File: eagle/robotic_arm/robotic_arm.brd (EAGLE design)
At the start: 81.3 x 63.5 mm, 98 parts, among them J2 (ID,OD)=(2.1,5.5)MM, SW1 5A/28V, Y1 16MHz

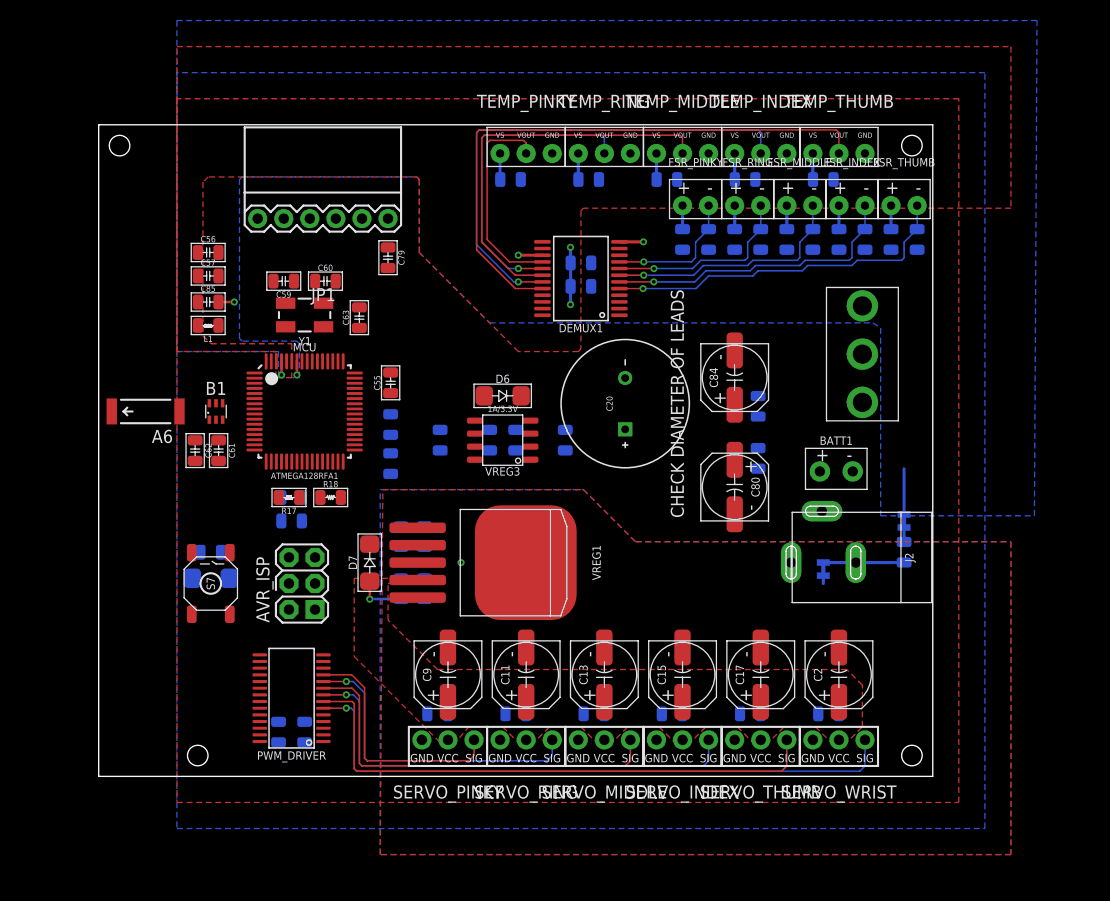
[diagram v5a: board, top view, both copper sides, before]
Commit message: Started on immediate power connections
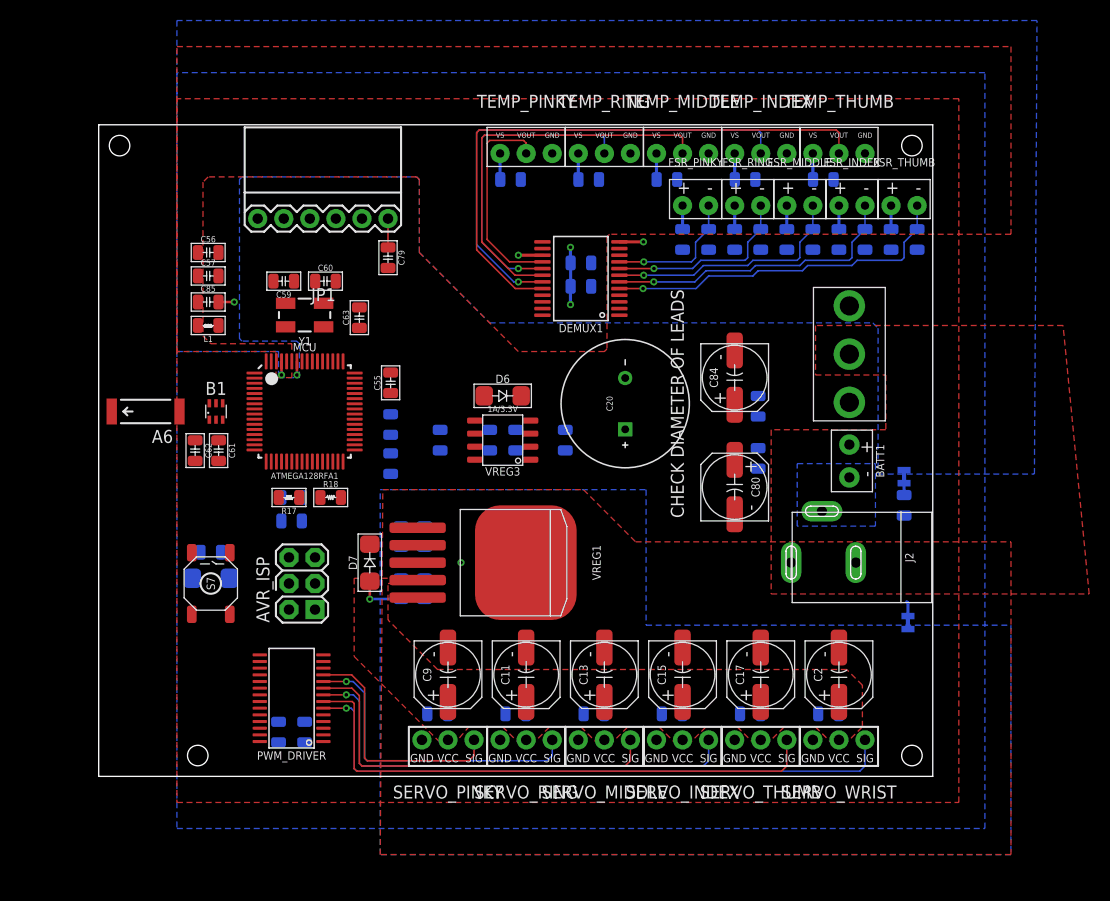
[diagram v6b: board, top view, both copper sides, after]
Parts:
- moved SUPPLY51 9.76 mm to (81.4, 15.0)
- moved L2 4.57 mm to (81.0, 26.4)
- moved SUPPLY52 4.32 mm to (81.0, 29.2)
- moved BATT1 1.63 mm to (75.7, 30.7), turned to 270 degrees
- moved SW1 1.27 mm to (75.7, 41.1)
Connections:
- net N$2 renamed BATT_-
- net N$43 renamed BATT_+
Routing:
- net GND: track 7.87 -> 1.45 mm
- net AGND: track 13.3 -> 9.01 mm
- net N$41: track 0.00 -> 2.81 mm
- net NGND: track 0.77 -> 0.00 mm
- added copper zone on layer 1, net BATT_+
- added copper zone on layer 16, net BATT_-

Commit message: Moved DEMUX to give some more power plane area.
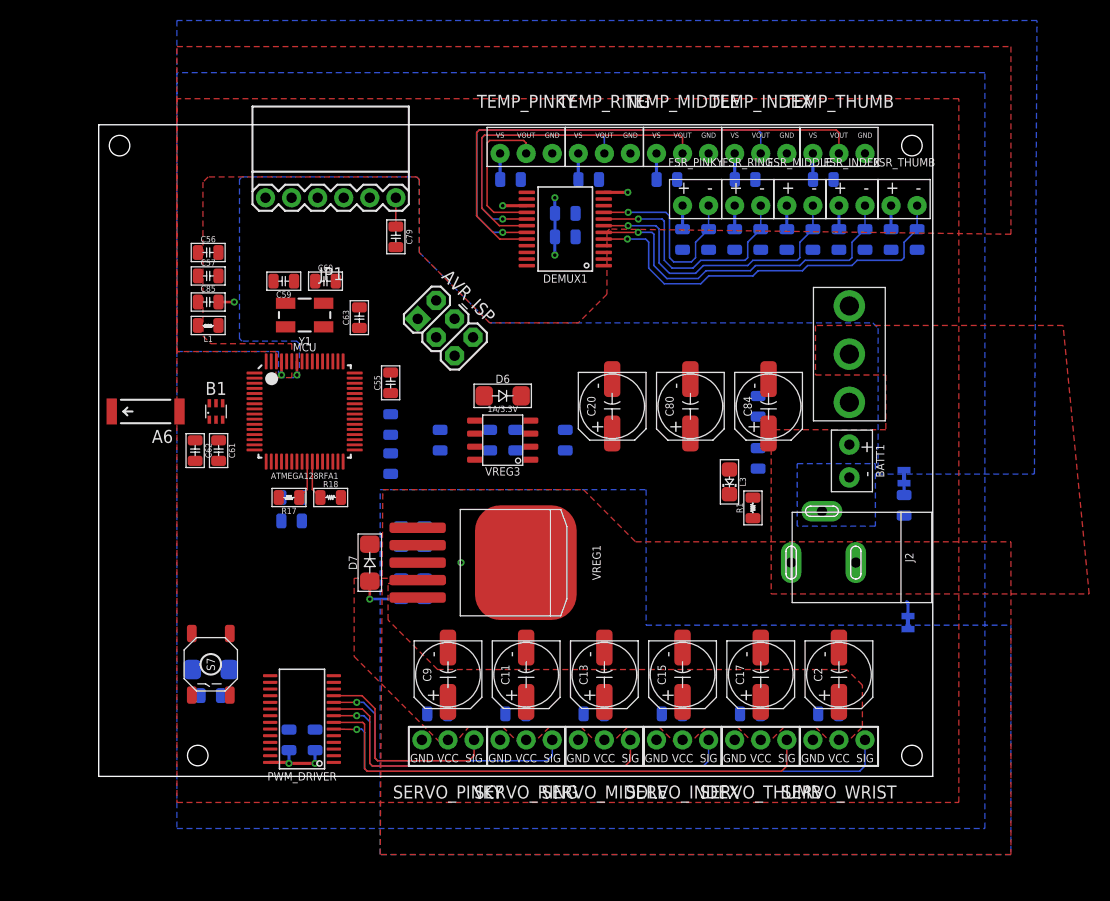
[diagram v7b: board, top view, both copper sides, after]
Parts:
- added L3: BLUE, MrSwirlyEyes:LED_SMD-805_
- added R1: 10KΩ, MrSwirlyEyes:RESISTOR_SMD-805
- C20: value 1000uF/50V -> 220uF/16V; device MrSwirlyEyes:CAP_POL_DIA12.5-LS5-H27 -> MrSwirlyEyes:CAP_POL_SMD_L6.6-W6.6
- moved AVR_ISP 28.5 mm to (36.3, 43.7), turned to 315 degrees
- moved R43 14.0 mm to (13.5, 7.87), turned to 0 degrees
- moved C80 8.98 mm to (60.2, 36.1), turned to 90 degrees
- moved D1 8.89 mm to (13.5, 10.4), turned to 0 degrees
- moved S7 7.87 mm to (13.5, 10.9), turned to 90 degrees
- moved C18 5.06 mm to (48.0, 54.9)
- moved C26 5.06 mm to (48.0, 52.6)
- moved DEMUX1 5.06 mm to (48.0, 53.3)
- moved C84 4.33 mm to (67.8, 36.1)
- moved PWM_DRIVER 2.27 mm to (22.4, 5.59)
- moved C79 2.17 mm to (31.5, 52.6)
- moved JP1 2.17 mm to (31.5, 56.4)
- moved C20 1.30 mm to (52.6, 36.1)
- moved C25 1.27 mm to (21.1, 3.56)
- moved C19 1.27 mm to (23.6, 3.56)
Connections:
- new net N$2: L3.K, R1.2
- net GND: now also C20.K, R1.1; no longer C20.-
- net N$1: now also C20.A, L3.A; no longer C20.+
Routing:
- net VCC: track 0.00 -> 6.98 mm, vias 0 -> 2
- net FSR_PINKY: track 13.2 -> 19.1 mm
- net FSR_RING: track 18.6 -> 24.3 mm
- net TEMP_PINKY: track 56.9 -> 51.5 mm
- net TEMP_THUMB: track 20.7 -> 15.3 mm
- net TEMP_MIDDLE: track 38.7 -> 33.2 mm
- net TEMP_INDEX: track 30.8 -> 25.3 mm
- net FSR_MIDDLE: track 23.9 -> 29.2 mm
- net TEMP_RING: track 48.8 -> 43.6 mm
- net FSR_INDEX: track 29.2 -> 34.3 mm
- net FSR_THUMB: track 34.6 -> 39.2 mm
- net SDA: track 0.00 -> 3.83 mm
- net SCL: track 0.00 -> 3.82 mm
- net SERVO_THUMB: track 31.0 -> 27.9 mm
- net SERVO_RING: track 54.4 -> 51.4 mm
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
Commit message: Routed VBATT and moved MCU regulator for a well-shaped power plane
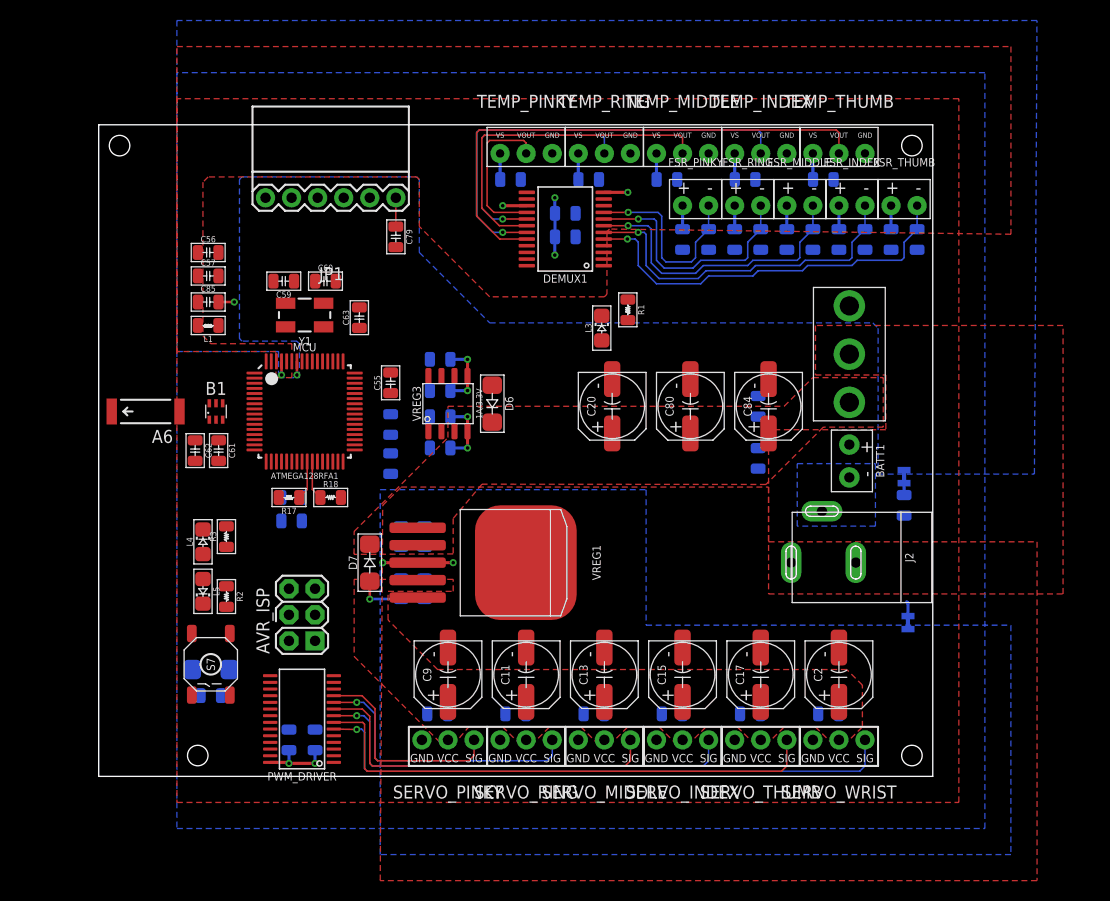
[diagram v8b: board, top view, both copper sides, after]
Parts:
- added L4: GREEN, MrSwirlyEyes:LED_SMD-805_
- added L5: RED, MrSwirlyEyes:LED_SMD-805_
- added R2: 2KΩ, MrSwirlyEyes:RESISTOR_SMD-805
- added R3: 1KΩ, MrSwirlyEyes:RESISTOR_SMD-805
- moved AVR_ISP 31.2 mm to (22.4, 15.7), turned to 90 degrees
- moved R1 22.8 mm to (54.1, 45.5), turned to 270 degrees
- moved L3 19.5 mm to (51.6, 43.7), turned to 90 degrees
- moved C96 12.4 mm to (35.8, 35.1), turned to 0 degrees
- moved C92 9.24 mm to (35.8, 40.6), turned to 0 degrees
- moved C95 7.41 mm to (35.8, 32.0), turned to 0 degrees
- moved VREG3 6.41 mm to (36.6, 36.3), turned to 90 degrees
- moved C93 4.83 mm to (35.8, 37.6), turned to 0 degrees
- moved D6 1.27 mm to (40.9, 36.3), turned to 270 degrees
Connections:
- net N$1 renamed VBATT
- removed net S0: DEMUX1.10
- removed net S1: DEMUX1.11
- removed net S2: DEMUX1.14
- removed net S3: DEMUX1.13
- removed net SIG: DEMUX1.1
- new net N$3: L4.K, R3.2
- new net N$5: L5.K, R2.2
- net A0: now also DEMUX1.1
- net GND: now also R2.1, R3.1
- net PB6: now also L5.A
- net PB7: now also L4.A
- net PE2: now also DEMUX1.10
- net PE6: now also DEMUX1.11
- net PE7: now also DEMUX1.14
- net SSN: now also DEMUX1.13
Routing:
- net NGND: track 0.00 -> 6.86 mm, vias 0 -> 2
- net VBATT: track 0.00 -> 6.38 mm, vias 0 -> 2
- net VCC: track 6.98 -> 13.4 mm, vias 2 -> 4
- added copper zone on layer 1, net VBATT
